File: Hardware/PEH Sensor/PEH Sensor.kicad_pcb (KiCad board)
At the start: 2 copper layers, 39.4 x 65 mm, 45 parts, among them J1 JST-XH-A B3B, Q1 AO3401A, SW1 JS202011JCQN, U1 SHTC3, U2 BQ25570, U3 VEML7700-TR, U4 INA226, U5 ESP32S3 Super Mini

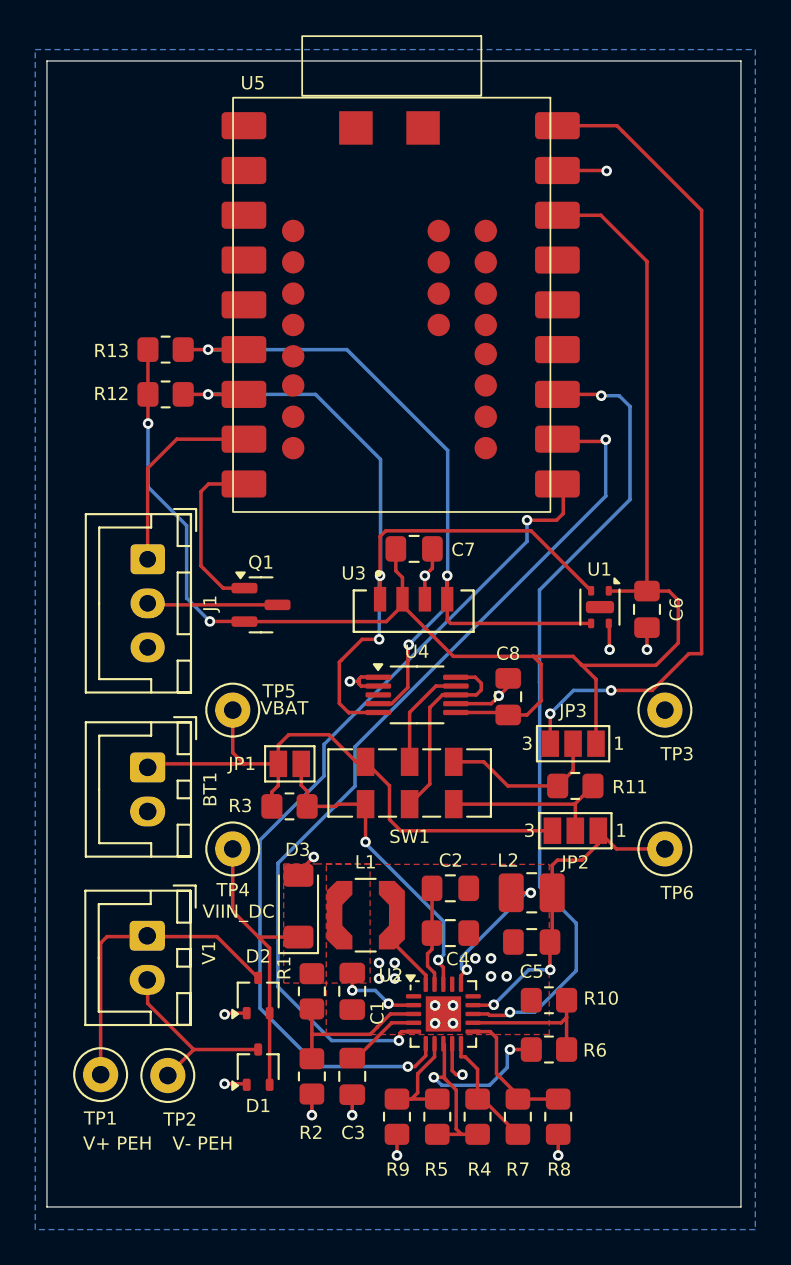
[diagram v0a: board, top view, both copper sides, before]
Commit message: Several PCB updates to hardware. Started BLE app on androidstudio.
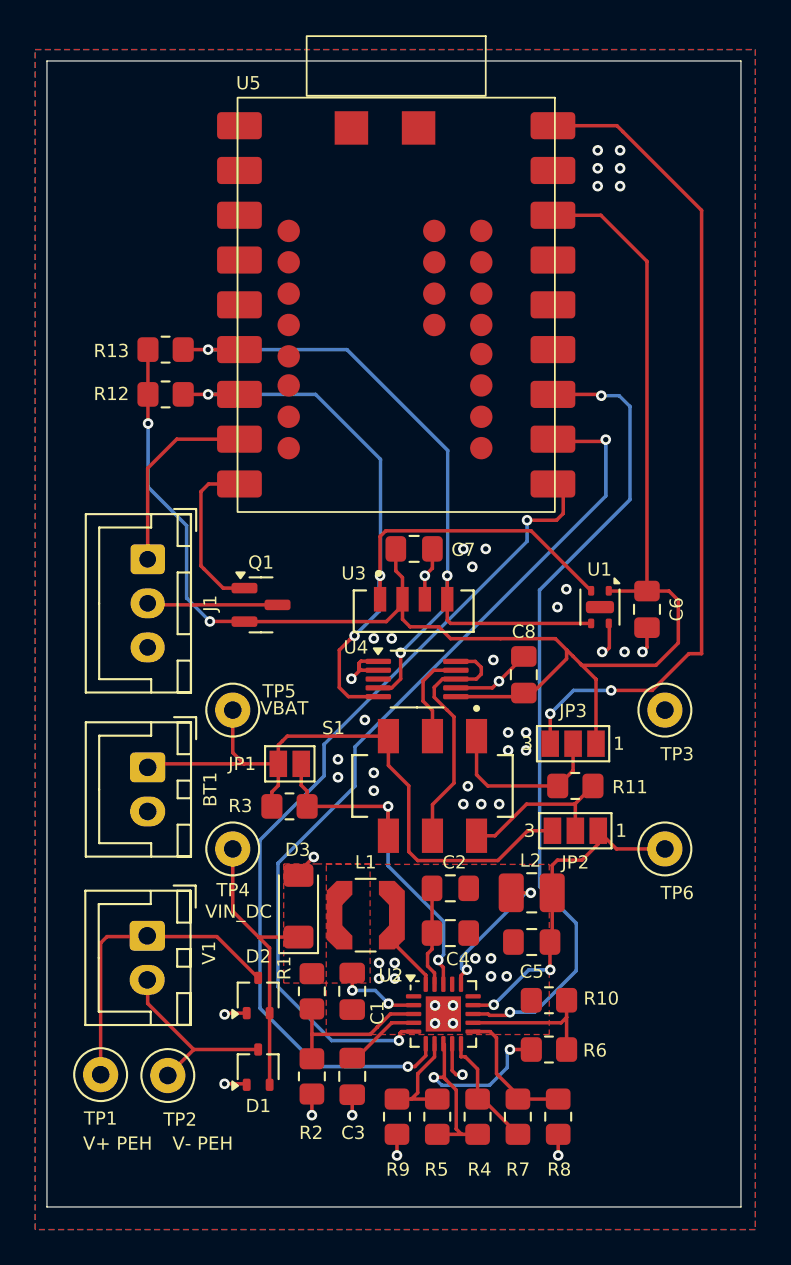
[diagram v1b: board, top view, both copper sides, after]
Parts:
- removed SW1: JS202011JCQN, Button_Switch_SMD:SW_DPDT_CK_JS202011JCQN
- added S1: SLW-913535-2A-SMT, SLW-913535-2A-SMT:SW_SLW-913535-2A-SMT, F.Cu at (148.6, 99.3)
- L1: value 22uH -> LPS4018-223M
- L2: value 10uH -> DFE252012C-H-100M
- Q1: value AO3401A -> IRLML6402TRPBF
- moved C8 1.53 mm to (153.8, 93.0)
- moved U4 0.90 mm to (147.7, 93.2)
- moved U5 0.25 mm to (146.6, 72.0)
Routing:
- net /VPHE-: track 33.6 -> 37.0 mm
- net Net-(U4-Vbus): track 11.2 -> 14.3 mm
- net /VPHE+: track 18.2 -> 20.5 mm
- net /SCL: track 49.6 -> 48.2 mm
- net GND: track 26.7 -> 25.5 mm, vias 26 -> 53
- net /SDA: track 46.6 -> 45.7 mm
- net /Vout_shunt-: track 9.22 -> 9.82 mm
- net Net-(U4-Vin-): track 6.05 -> 5.46 mm
- net +3V3: track 93.4 -> 94.0 mm
- net /Vout_shunt+: track 9.87 -> 9.31 mm

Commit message: Programa de prueba de sensores y actualización de PCB con cambio en la librería del VEML770
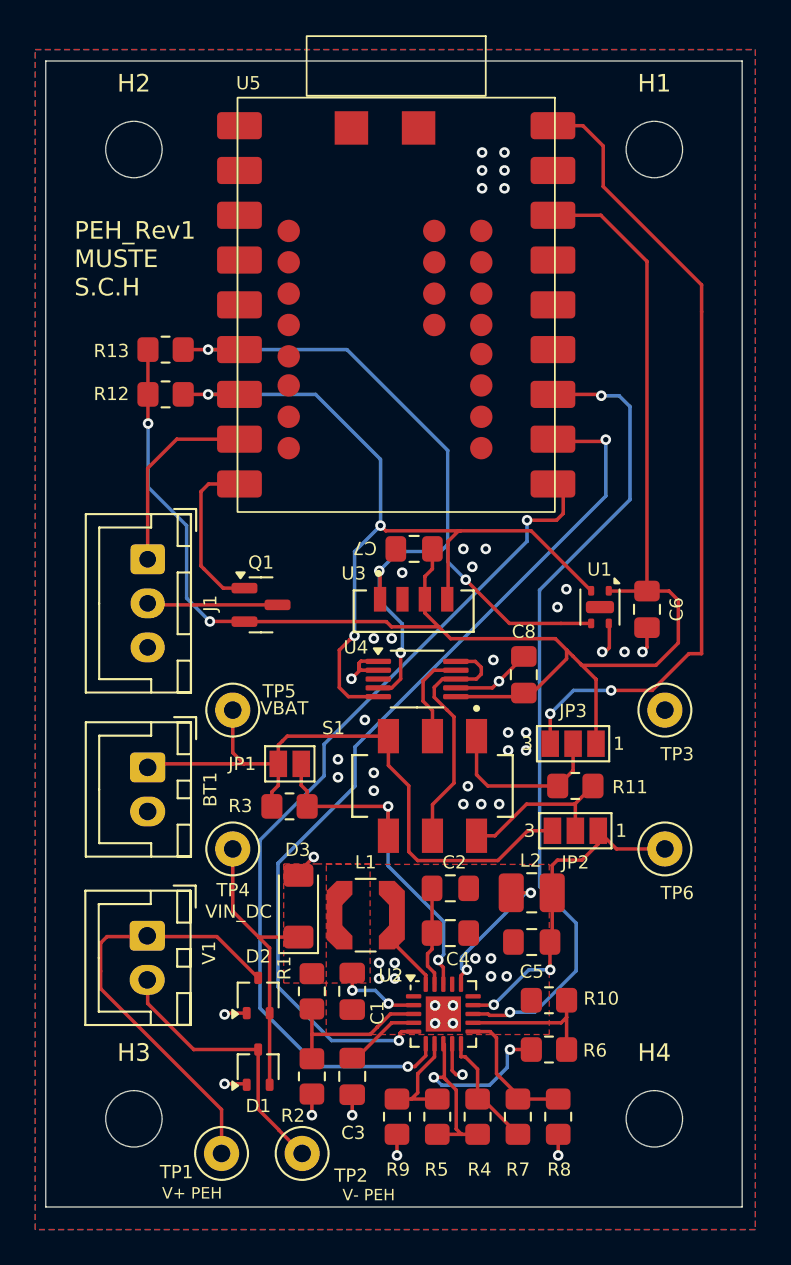
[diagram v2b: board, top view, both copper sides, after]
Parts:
- added H1: MountingHole, MountingHole:MountingHole_3.2mm_M3_DIN965, F.Cu at (161.2, 63.2)
- added H2: MountingHole, MountingHole:MountingHole_3.2mm_M3_DIN965, F.Cu at (131.7, 63.2)
- added H3: MountingHole, MountingHole:MountingHole_3.2mm_M3_DIN965, F.Cu at (131.7, 118.2)
- added H4: MountingHole, MountingHole:MountingHole_3.2mm_M3_DIN965, F.Cu at (161.2, 118.2)
- moved TP2 8.81 mm to (141.2, 120.1)
- moved TP1 8.19 mm to (136.7, 120.1)
- turned C7 to 180 degrees
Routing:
- net Net-(D2-COM): track 17.5 -> 24.8 mm
- net Net-(D1-COM): track 10.7 -> 15.6 mm
- net /SDA: track 45.7 -> 49.6 mm, vias 3 -> 4
- net GND: track 25.5 -> 23.1 mm
- net +5V: track 47.0 -> 46.1 mm
- net /SCL: track 48.2 -> 48.8 mm
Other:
- board size 39.4 x 65 mm -> 39.5 x 65 mm
- board text added: "PEH_Rev1 MUSTE S.C.H"
